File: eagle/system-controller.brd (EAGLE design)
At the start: 99 x 100 mm, 235 parts, among them CN1 22u, IC1 TS4100, J1 1, Q0 MOSFET-P-N-PAIR, Q1 MOSFET-P-N-PAIR, Q10 DNP/NTR4101P, Q11 DNP/NTR4101P, Q12 DNP/NTR4101P, Q13 DON3035L, Q2 MOSFET-P-N-PAIR, Q3 MOSFET-P-N-PAIR, Q4 MOSFET-P-N-PAIR, Q5 MOSFET-P-N-PAIR, Q6 MOSFET-P-N-PAIR, Q7 MOSFET-P-N-PAIR, Q9 DNP/NTR4101P, SW0 TPS25944LRVCRWQFN-20-3X4, SW1 TPS25944LRVCRWQFN-20-3X4, SW2 TPS25944LRVCRWQFN-20-3X4, SW3 TPS25944LRVCRWQFN-20-3X4, SW4 TPS25944LRVCRWQFN-20-3X4, SW5 TPS25944LRVCRWQFN-20-3X4, SW6 TPS25944LRVCRWQFN-20-3X4, SW7 TPS25944LRVCRWQFN-20-3X4, U1 MEGA128-A, X1 8 MHz CRYSTAL-ABRACON-ABM3-SMD

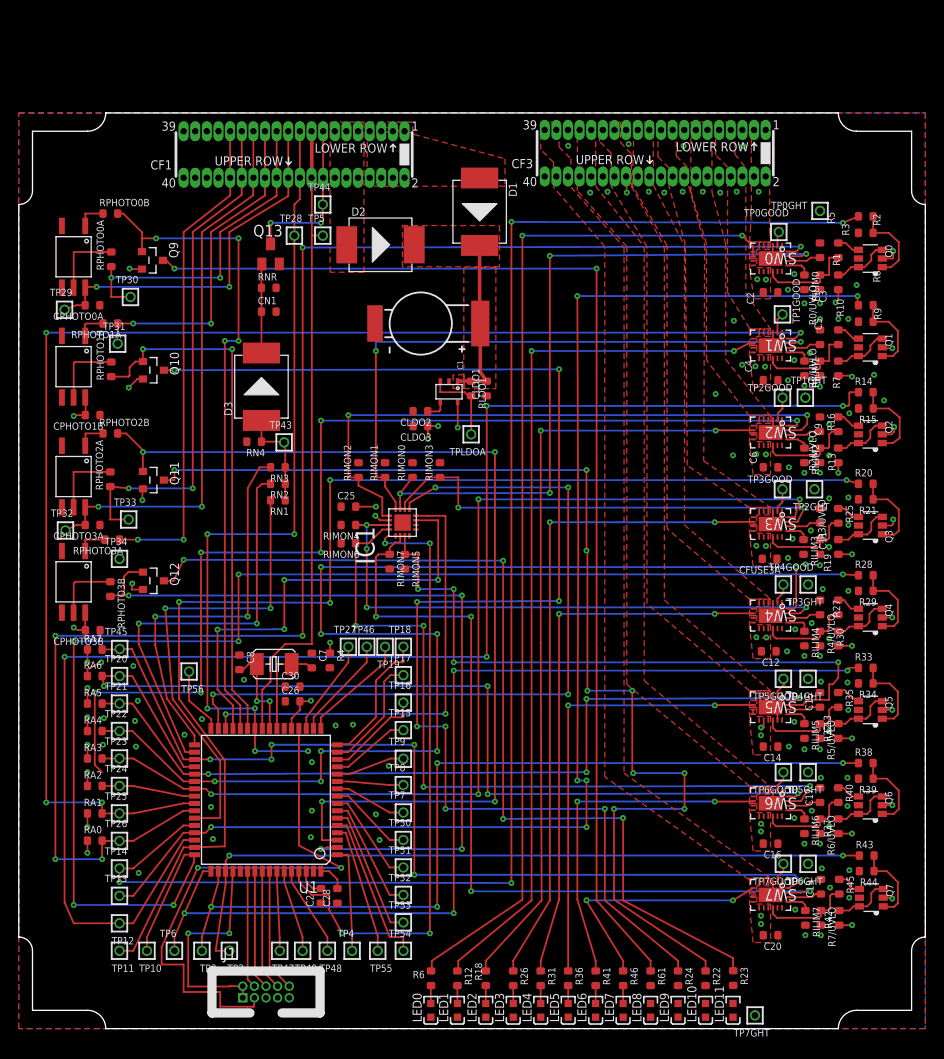
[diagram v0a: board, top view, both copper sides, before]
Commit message: made polygons wider and changed physical layout of them. Also, reduced space between traces
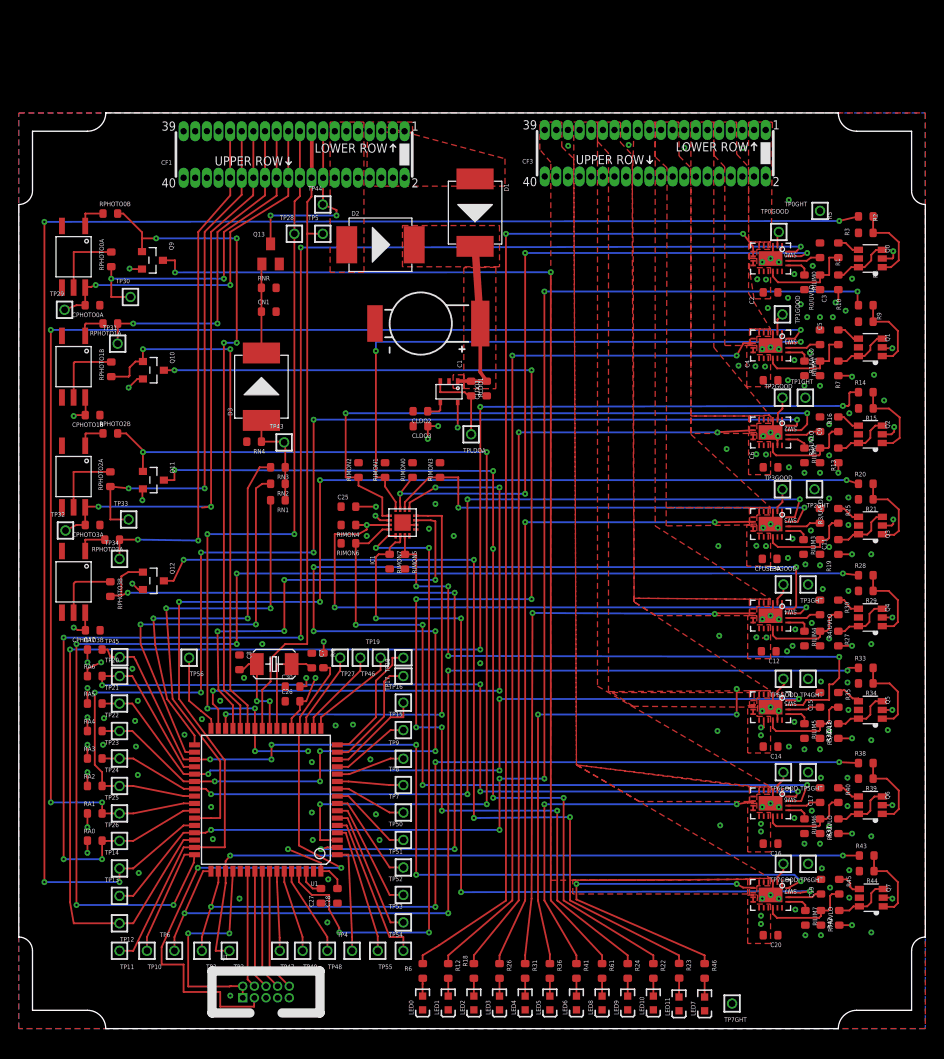
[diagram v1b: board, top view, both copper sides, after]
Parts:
- RIMON0, RIMON1, RIMON2, RIMON3, RIMON4, RIMON5, RIMON6, RIMON7: value 47k -> 30k
- moved R46 8.94 mm to (74.9, 6.30)
- moved LED7 8.93 mm to (74.9, 2.70)
- moved R23 5.95 mm to (72.1, 6.32)
- moved LED11 5.94 mm to (72.1, 2.70)
- moved LED10 5.76 mm to (69.3, 2.80)
- moved R22 5.76 mm to (69.3, 6.30)
- moved LED9 5.56 mm to (66.5, 2.80)
- moved R24 5.56 mm to (66.5, 6.30)
- moved LED8 5.36 mm to (63.7, 2.80)
- moved R61 5.36 mm to (63.7, 6.30)
- moved TP7GHT 2.82 mm to (77.9, 2.74)
- moved LED6 2.25 mm to (60.9, 2.80)
- moved R41 2.25 mm to (60.9, 6.30)
- moved LED5 2.15 mm to (58.0, 2.80)
- moved R36 2.15 mm to (58.0, 6.30)
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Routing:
- net N$55: track 155.1 -> 97.3 mm
- net N$54: track 125.6 -> 104.0 mm, vias 9 -> 5
- net VCB0_EN: track 164.5 -> 180.7 mm
- net N$48: track 83.9 -> 68.9 mm
- net N$61: track 148.5 -> 136.7 mm
- net VCB7: track 27.5 -> 37.4 mm
- net N$15: track 60.8 -> 69.3 mm
- net 3V: track 68.7 -> 76.7 mm, vias 23 -> 25
- net VCB4_IMON: track 68.2 -> 74.8 mm, vias 4 -> 3
- net N$58: track 126.7 -> 121.4 mm
- net GND: track 30.9 -> 34.3 mm, vias 93 -> 136
- net VCB6: track 38.0 -> 41.2 mm, vias 3 -> 2
- net VBUS: track 25.4 -> 28.5 mm
- net UART_LGR_TX: track 54.1 -> 56.7 mm
- net NUCLEAROPTION_OUT: track 18.6 -> 21.3 mm
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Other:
- board text removed: "Note: Look for hidden air wires"

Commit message: latest updates added
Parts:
- RN4: value 10k -> 390
- moved R4 0.45 mm to (32.9, 40.0)
- moved C7 0.45 mm to (31.6, 40.0)
- moved C6 0.22 mm to (82.0, 61.1)
- moved C12 0.20 mm to (81.9, 41.0)
- moved C2 0.20 mm to (82.1, 80.2)
- moved C4 0.20 mm to (82.1, 70.6)
- moved C26 0.20 mm to (29.7, 35.8)
- moved C30 0.20 mm to (29.7, 37.4)
- moved CPHOTO3B 0.20 mm to (8.28, 43.5)
- moved CFUSE3A 0.20 mm to (82.0, 51.1)
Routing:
- net I2C-SDA: track 88.4 -> 80.2 mm, vias 6 -> 4
- net 3V: track 76.7 -> 77.4 mm
- net GND: vias 136 -> 228

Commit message: newest changes
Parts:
- removed IC1: TS4100, TQFN16300x300:QFN50P400X400X80-17N
- added IC2: TS4100, system-controller:QFN50P400X400X80-17N
- D1, D2, D3: device SMD-DIODE-SCHOTTKY-40V-5A_DO-214AB_ SSC53L:DO-214AB -> system-controller:DO-214AB
- SW0, SW1, SW2, SW3, SW4, SW5, SW6, SW7: device WQFN-20-3x4:QFN-20-L -> system-controller:QFN-20-L
- moved TP7GHT 17.4 mm to (93.1, 11.2), turned to 0 degrees
- moved D1 1.46 mm to (48.6, 89.9)
- moved R4 0.40 mm to (33.3, 40.0)
- moved TP47 0.27 mm to (28.2, 8.50)
- moved D2 0.10 mm to (39.5, 85.5)
- moved SW5 0.10 mm to (82.0, 35.1)
- moved SW7 0.10 mm to (82.0, 14.6)
- turned TP17 to 180 degrees
- turned TP18 to 180 degrees
- renumbered CPHOTO0A to C31, CPHOTO1B to C32, CPHOTO3A to C33, CPHOTO3B to C34, RPHOTO0A to R47, RPHOTO0B to R49, RPHOTO1A to R48, RPHOTO1B to R50, RPHOTO2A to R51, RPHOTO2B to R54, RPHOTO3A to R52, RPHOTO3B to R53
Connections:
- net 3V: now also IC2.14; no longer IC1.14
- net GND: now also IC2.17, IC2.4, IC2.6; no longer IC1.17, IC1.4, IC1.6
- net N$107: now also IC2.1; no longer IC1.1
- net N$46: now also IC2.7; no longer IC1.7
- net N$47: now also IC2.8; no longer IC1.8
- net N$48: now also IC2.9; no longer IC1.9
- net VCB0_IMON: now also IC2.11; no longer IC1.11
- net VCB1_IMON: now also IC2.12; no longer IC1.12
- net VCB2_IMON: now also IC2.13; no longer IC1.13
- net VCB3_IMON: now also IC2.10; no longer IC1.10
- net VCB4_IMON: now also IC2.15; no longer IC1.15
- net VCB5_IMON: now also IC2.3; no longer IC1.3
- net VCB6_IMON: now also IC2.16; no longer IC1.16
- net VCB7_IMON: now also IC2.2; no longer IC1.2
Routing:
- net VCB4_IMON: track 74.8 -> 69.6 mm
- net VBUS: track 28.4 -> 24.1 mm
- net VCB4: track 62.4 -> 58.6 mm
- net GND: track 34.3 -> 36.3 mm, vias 228 -> 287
- net VCB0: track 113.3 -> 112.3 mm
- net N$15: track 69.0 -> 68.1 mm
- net V+: track 19.9 -> 20.7 mm
- net N$47: track 49.7 -> 49.0 mm
- net 3V: track 77.4 -> 78.0 mm, vias 25 -> 24

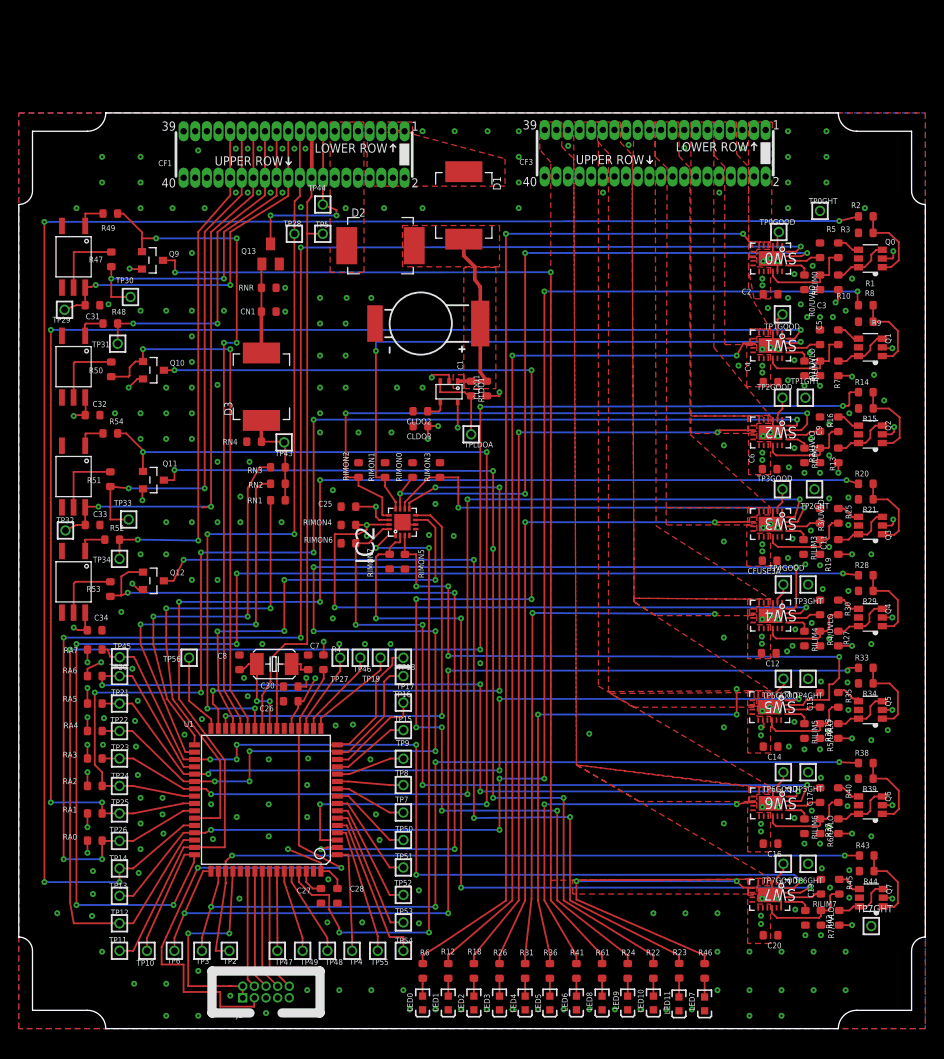
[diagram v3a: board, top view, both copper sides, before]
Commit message: final changes pushed for the day: change to optical isolation circuitry and board fixes due to this
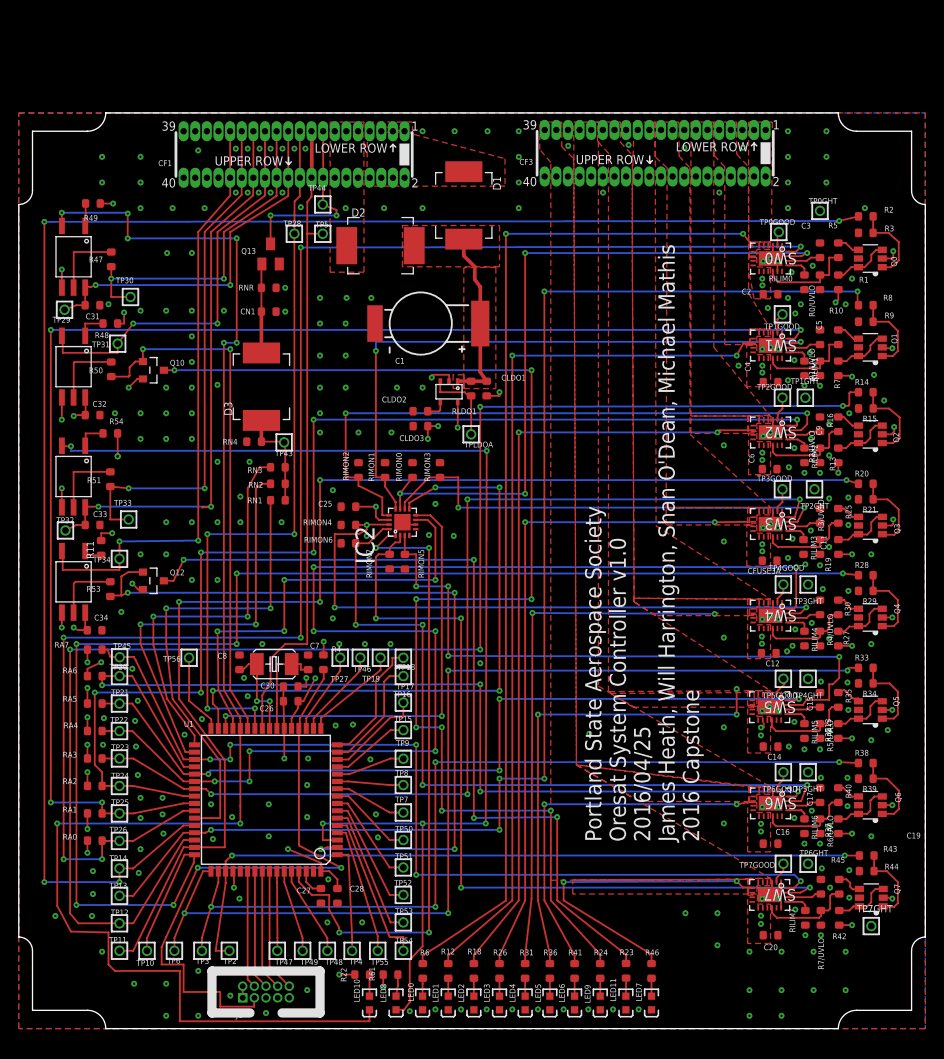
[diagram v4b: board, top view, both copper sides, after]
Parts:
- removed Q11, Q9: DNP/NTR4101P, Tova:SOT23
- removed R52: 390, rcl_custom:.0603-B-NOSILK
- added R11: 390, rcl_custom:.0603-B-NOSILK
- moved R22 31.8 mm to (37.5, 5.90), turned to 0 degrees
- moved LED10 31.0 mm to (38.3, 2.80)
- moved R61 23.1 mm to (40.6, 5.90), turned to 0 degrees
- moved LED8 22.5 mm to (41.2, 2.80)
- moved LED7 5.80 mm to (69.1, 2.80)
- moved LED11 5.80 mm to (66.3, 2.80)
- moved R23 5.80 mm to (66.3, 6.32)
- moved R46 5.80 mm to (69.1, 6.30)
- moved LED9 3.00 mm to (63.5, 2.80)
- moved R24 3.00 mm to (63.5, 6.30)
- moved R49 2.20 mm to (8.10, 90.1)
- moved LED6 0.20 mm to (60.7, 2.80)
- moved R41 0.20 mm to (60.7, 6.30)
- turned R48 to 0 degrees
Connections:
- removed net N$20: R52.2, U$4.1
- removed net N$58 (its old number): Q9.3, R61.1
- net 3V: now also R11.2, R22.1, R48.2, R49.2, R54.2, R61.1; no longer Q11.2, Q9.2
- net GND: no longer LED10.K, LED8.K, U$1.2, U$2.2, U$3.2, U$4.2
- net N$54: now also R11.1, U$4.1; no longer Q11.3, R22.1
- net N$8: now also R48.1; no longer R48.2
- net TXD0: now also LED8.K, U$3.2; no longer Q11.1, R54.2
- net TXD1: now also LED10.K, U$1.2; no longer Q9.1, R49.2
- net UART_FC_TX: now also U$2.2; no longer R48.1
- net UART_LGR_TX: now also U$4.2; no longer R52.1
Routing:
- net N$58 (its old number): track 121.4 -> 0.00 mm, vias 2 -> 0
- net N$54: track 104.0 -> 2.20 mm, vias 5 -> 0
- net TXD1: track 71.4 -> 164.5 mm, vias 4 -> 8
- net TXD0: track 105.8 -> 130.8 mm, vias 4 -> 5
- net GND: track 36.3 -> 52.2 mm, vias 287 -> 280
- net 3V: track 78.0 -> 64.9 mm, vias 24 -> 28
- net UART_LGR_TX: track 56.7 -> 66.1 mm
- net UART_FC_TX: track 36.7 -> 44.5 mm
- net N$55: track 97.3 -> 92.2 mm
- net N$20: track 3.37 -> 0.00 mm
- net VCB7: track 37.9 -> 35.4 mm
- net N$61: track 136.7 -> 134.4 mm
- net N$58: track 3.29 -> 2.50 mm
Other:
- board text added: "Portland State Aerospace Society Oresat System Controller v1.0 2016/04/25 James Heath, Will Harrington, Shan O'Dean, Michael Mathis 2016 Capstone"

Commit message: I lied. 1 more
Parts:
- moved R22 4.80 mm to (42.3, 5.90), turned to 270 degrees
- moved R61 4.71 mm to (45.3, 6.20), turned to 270 degrees
- moved LED10 4.00 mm to (42.3, 2.70)
- moved LED8 4.00 mm to (45.2, 2.70)
- moved LED11 3.90 mm to (70.2, 2.70)
- moved LED4 3.90 mm to (59.2, 2.70)
- moved LED7 3.90 mm to (73.0, 2.70)
- moved LED9 3.90 mm to (67.4, 2.70)
- moved R23 3.90 mm to (70.2, 6.22)
- moved R24 3.90 mm to (67.4, 6.20)
- moved R31 3.90 mm to (59.2, 6.20)
- moved R46 3.90 mm to (73.0, 6.20)
- moved R6 3.90 mm to (48.0, 6.20)
- moved LED0 3.90 mm to (48.0, 2.70)
- moved LED1 3.90 mm to (50.8, 2.70)
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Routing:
- net TXD1: track 164.5 -> 168.4 mm
- net VCB7: track 35.4 -> 38.8 mm
- net N$55: track 92.2 -> 95.6 mm
- net N$61: track 134.4 -> 137.4 mm
- net VCB0: track 112.3 -> 109.4 mm
- net VCB6: track 41.0 -> 43.6 mm
- net VCB1: track 96.3 -> 93.9 mm
- net VCB5: track 51.8 -> 53.7 mm
- net VCB2: track 85.8 -> 84.2 mm
- net VCB4: track 58.6 -> 59.4 mm
- net N$56: track 2.35 -> 1.65 mm
- net 3V: track 64.9 -> 65.4 mm

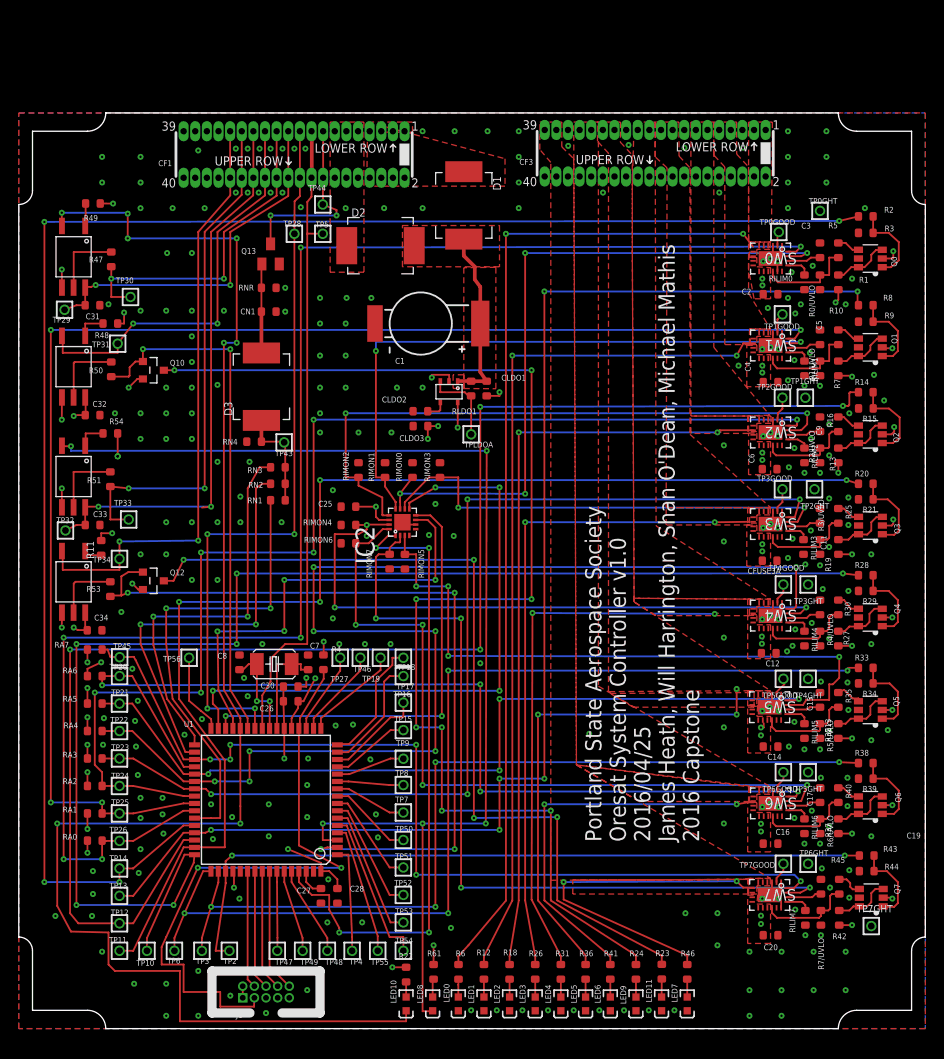
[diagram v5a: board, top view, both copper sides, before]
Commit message: Better layout for bypass caps ner AVR. Some cleanup on routing. Changed power domain indicators to DNP.
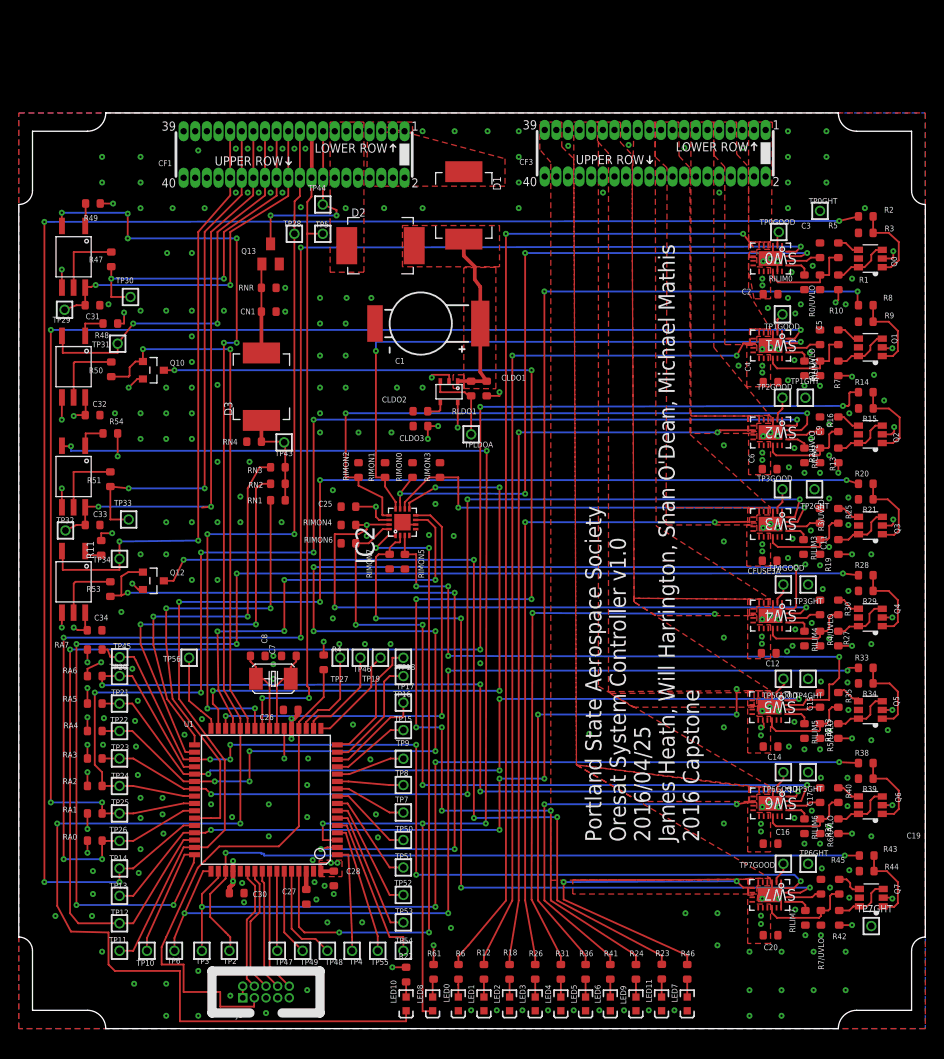
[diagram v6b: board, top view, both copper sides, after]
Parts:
- LED0, LED1, LED2, LED3, LED4, LED5, LED6, LED7: value GRN -> DNP/GRN
- R12, R18, R26, R31, R36, R41, R46, R6: value 1k -> DNP/1k
- moved C30 23.3 mm to (23.8, 14.8), turned to 180 degrees
- moved C7 2.21 mm to (29.5, 40.7), turned to 0 degrees
- moved C8 2.12 mm to (26.1, 40.7), turned to 180 degrees
- moved C28 1.94 mm to (34.4, 16.4)
- moved C27 1.60 mm to (31.4, 14.4)
- moved X1 1.60 mm to (27.8, 38.2)
- moved C26 0.95 mm to (29.7, 34.8)
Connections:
- net N$36 renamed AREF
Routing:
- net N$15: track 68.1 -> 58.3 mm, vias 2 -> 0
- net 3V: track 65.4 -> 58.8 mm, vias 28 -> 29
- net GND: track 52.2 -> 47.7 mm, vias 280 -> 283
- net I2C-SCL: track 70.3 -> 72.2 mm, vias 0 -> 2
- net N$17: track 11.0 -> 9.25 mm
- net N$1: track 10.8 -> 9.24 mm, vias 2 -> 0
- net VCB6_EN: track 95.5 -> 96.9 mm
- net N$37: track 9.83 -> 11.2 mm
- net N$107: track 69.7 -> 71.0 mm
- net PCB3_EN: track 134.6 -> 133.5 mm
- net AREF: track 3.08 -> 1.99 mm
- net N$27: track 9.80 -> 10.8 mm
- net VCB7_EN: track 80.8 -> 81.9 mm
- net N$28: track 9.07 -> 9.95 mm
- net N$12: track 13.1 -> 13.9 mm
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- added copper zone on layer 1, net 3V

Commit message: Board cleanup.
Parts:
- moved TP29 4.75 mm to (9.10, 80.9)
- moved TP32 4.60 mm to (8.90, 57.0)
- moved TP30 4.12 mm to (12.6, 84.0)
- moved TP33 3.60 mm to (12.0, 59.2)
- moved TP34 2.00 mm to (11.0, 53.3)
- moved R49 1.89 mm to (8.90, 88.4), turned to 90 degrees
- moved C34 1.78 mm to (6.50, 43.6), turned to 0 degrees
- moved C32 1.56 mm to (6.50, 67.0), turned to 0 degrees
- moved C33 1.56 mm to (6.50, 55.0), turned to 0 degrees
- moved C31 1.55 mm to (6.50, 79.0), turned to 0 degrees
- moved R54 1.34 mm to (8.80, 64.4), turned to 90 degrees
- moved R48 1.26 mm to (8.80, 76.6), turned to 90 degrees
- moved R50 0.82 mm to (10.3, 72.8), turned to 180 degrees
- moved R53 0.58 mm to (9.70, 48.5), turned to 0 degrees
- moved R11 0.40 mm to (9.00, 52.9)
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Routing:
- net GND: track 47.7 -> 39.6 mm, vias 283 -> 285
- net 3V: track 58.8 -> 51.5 mm, vias 29 -> 31
- net UART_LGR_RX: track 56.6 -> 50.8 mm, vias 2 -> 1
- net UART_FC_RX: track 36.8 -> 32.2 mm, vias 2 -> 1
- net RXD1: track 57.5 -> 53.7 mm
- net UART_LGR_VCC: track 62.1 -> 58.8 mm, vias 2 -> 1
- net N$5: track 7.99 -> 5.31 mm
- net UART_FC_VCC: track 40.6 -> 38.5 mm, vias 2 -> 1
- net N$18: track 7.24 -> 5.28 mm
- net N$4: track 3.29 -> 1.57 mm
- net N$8: track 3.29 -> 1.66 mm
- net RXD0: track 86.7 -> 85.1 mm
- net N$24: track 7.92 -> 6.44 mm
- net UART_LGR_TX: track 66.1 -> 64.8 mm, vias 2 -> 1
- net N$58: track 2.50 -> 1.67 mm
